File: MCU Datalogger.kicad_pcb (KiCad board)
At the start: 2 copper layers, 61 x 40.6 mm, 29 parts, among them J1 Conn_01x04_Pin, J2 Conn_01x04_Pin, J3 Conn_01x09_Pin, J4 Conn_02x03_Odd_Even, U1 24LC1025, U2 24LC1025, U3 DS1337S_, U4 ATMEGA328P-AU, Y1 16MHz, Y2 32.768 KHz

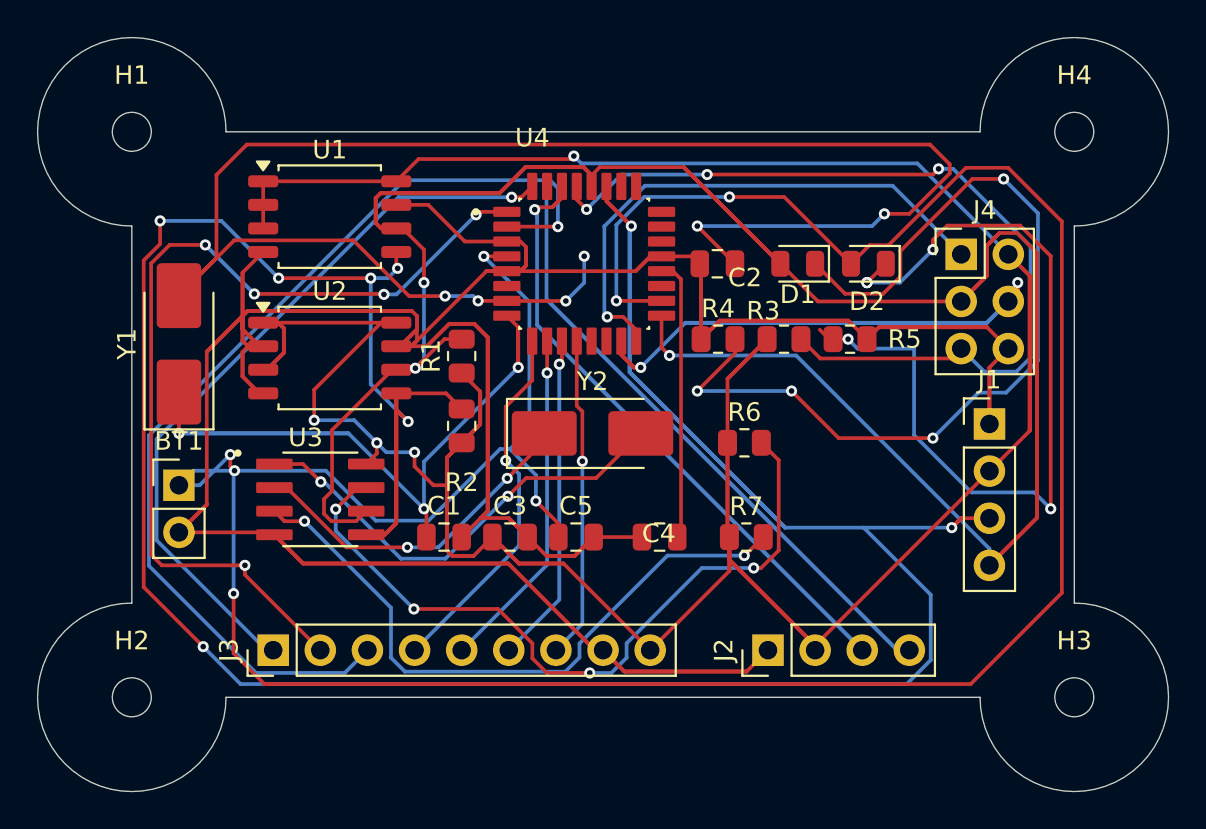
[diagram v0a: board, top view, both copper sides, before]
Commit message: Final 2-layered PCB with Logo
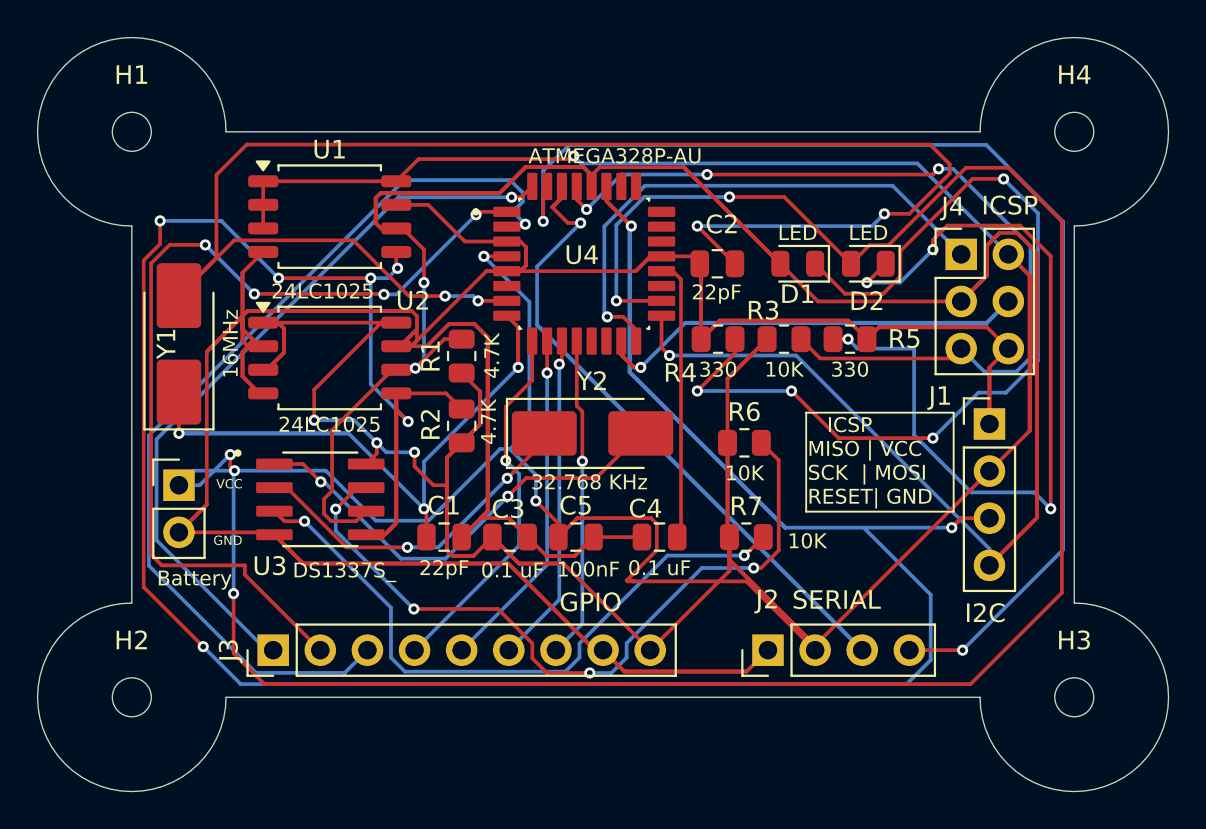
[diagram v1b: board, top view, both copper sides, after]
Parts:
- added REF**: KiCad-Logo2_12mm_SilkScreen, Symbol:KiCad-Logo2_12mm_SilkScreen, B.Cu at (109.5, 74.3)
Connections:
- BT1 pad 1: Net-(BT1-+) -> /VCC
- C5 pad 1: Net-(BT1-+) -> /VCC
- D2 pad 2: Net-(BT1-+) -> /VCC
- U4 pad 18: Net-(BT1-+) -> /VCC
- U4 pad 4: Net-(BT1-+) -> /VCC
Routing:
- net /VCC: track 201.0 -> 380.0 mm, vias 4 -> 11
- net Net-(BT1-+): track 157.5 -> 0.00 mm, vias 7 -> 0
- net Net-(U4-PB6): track 92.4 -> 86.4 mm, vias 6 -> 4
- net /TX: track 61.4 -> 65.2 mm, vias 0 -> 2
- net /D4: track 54.4 -> 50.9 mm
- net /RX: track 60.1 -> 61.2 mm
- net /MOSI: track 44.3 -> 43.3 mm, vias 2 -> 1
- net Net-(D2-K): track 46.4 -> 45.7 mm, vias 5 -> 4
- net /D3: vias 5 -> 4
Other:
- board text added: "* 2Mbit EEPROM * RTC * I2C,SPI, GPIOs"
- board text added: "Data Logger with the ATMega328P"
- board text added: "GND"
- board text added: "GPIO"
- board text added: "I2C"
- board text added: "ICSP"
- board text added: "ICSP MISO | VCC SCK | MOSI RESET| GND"
- board text added: "SERIAL"
- board text added: "VCC"

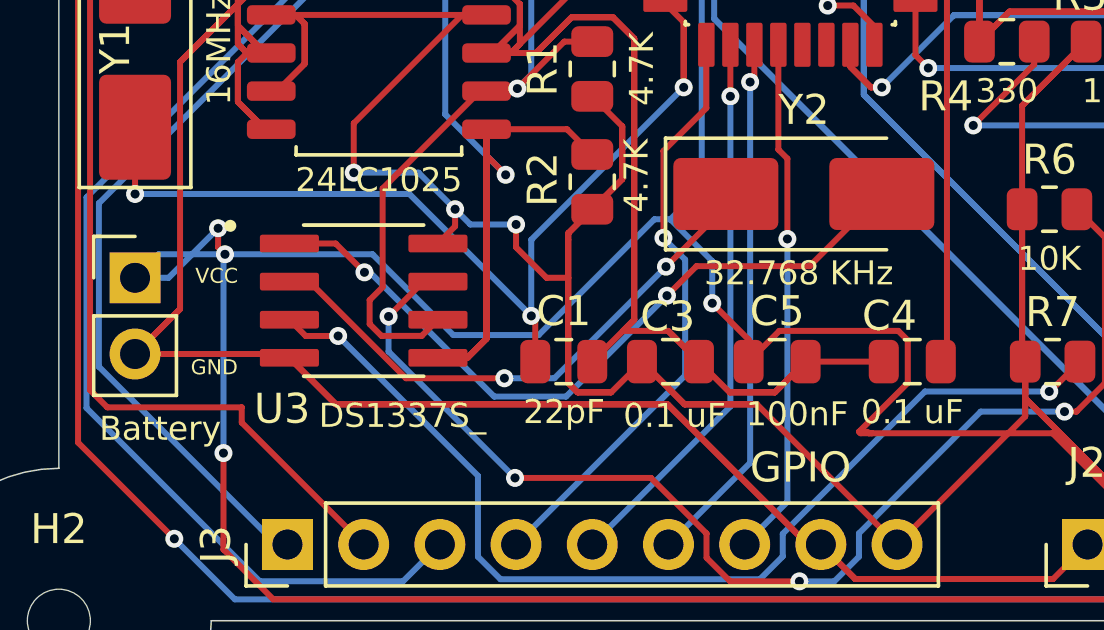
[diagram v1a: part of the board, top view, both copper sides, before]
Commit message: Completed 2-Layered PCB with Logo and 3D-shapes
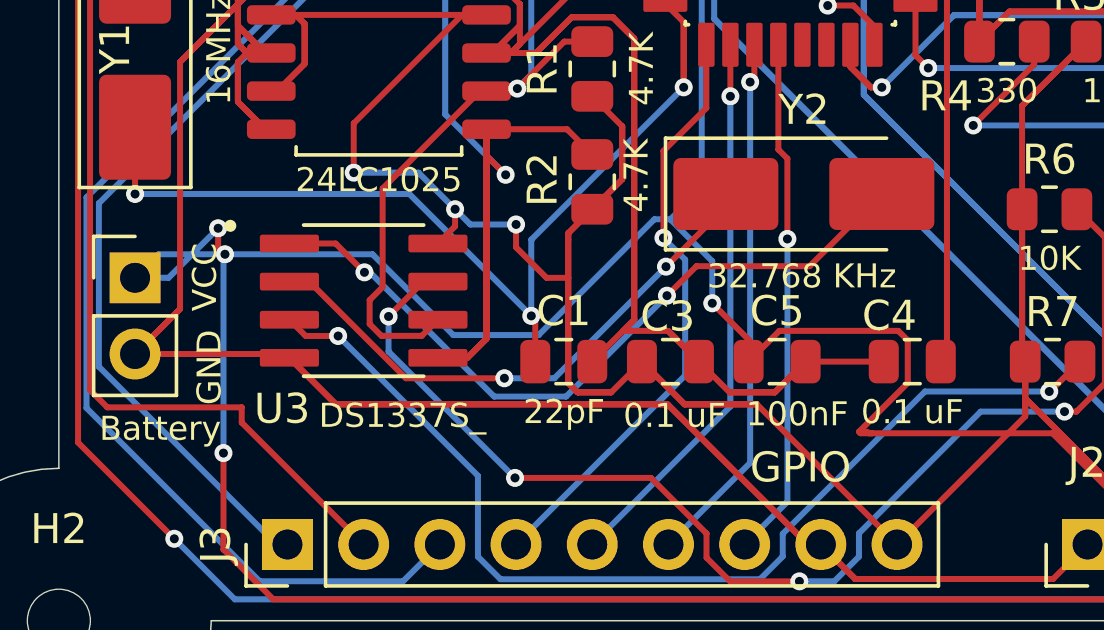
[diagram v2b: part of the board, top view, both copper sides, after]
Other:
- board text added: "By Josh"
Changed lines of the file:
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@@
 		)
 		(property "Value" "32.768 KHz"
-			(at -0.1686 2.6416 0)
+			(at -0.067 2.7432 0)
 			(layer "F.SilkS")
 			(effects
@@
 		)
 		(embedded_fonts no)
+		(model "${KICAD10_3DMODEL_DIR}/Package_SO.3dshapes/SOIC-8_3.9x4.9mm_P1.27mm.step"
+			(offset
+				(xyz 0 0 0)
+			)
+			(scale
+				(xyz 1 1 1)
+			)
+			(rotate
+				(xyz 0 0 0)
+			)
+		)
 	)
 	(footprint "Resistor_SMD:R_0805_2012Metric"
@@
 		)
 		(embedded_fonts no)
+		(model "${KICAD10_3DMODEL_DIR}/Package_QFP.3dshapes/TQFP-32_7x7mm_P0.8mm.step"
+			(offset
+				(xyz 0 0 0)
+			)
+			(scale
+				(xyz 1 1 1)
+			)
+			(rotate
+				(xyz 0 0 0)
+			)
+		)
 	)
 	(footprint "MountingHole:MountingHole_2.1mm"
@@
 		(layer "Edge.Cuts")
 	)
-	(gr_text "GND"
-		(at 85.6742 78.2066 0)
+	(gr_text "   ICSP\nMISO | VCC\nSCK  | MOSI\nRESET| GND"
+		(at 117.7036 76.0222 0)
 		(layer "F.SilkS")
 		(effects
 			(font
-				(size 0.5 0.5)
-				(thickness 0.01)
+				(size 0.8 0.8)
+				(thickness 0.1)
 			)
 			(justify left bottom)
 		)
 	)
-	(gr_text "VCC\n"
-		(at 85.8266 75.1586 0)
+	(gr_text "VCC"
+		(at 86.614 76.0476 90)
 		(layer "F.SilkS")
 		(effects
 			(font
-				(size 0.5 0.5)
-				(thickness 0.01)
+				(size 0.8 0.8)
+				(thickness 0.1)
 			)
 			(justify left bottom)
 		)
 	)
-	(gr_text "   ICSP\nMISO | VCC\nSCK  | MOSI\nRESET| GND"
-		(at 117.7036 76.0222 0)
+	(gr_text "GND"
+		(at 86.7664 79.1718 90)
 		(layer "F.SilkS")
 		(effects
@@
 	)
 	(gr_text "* 2Mbit EEPROM\n* RTC\n* I2C,SPI, GPIOs"
-		(at 124.1298 65.405 0)
+		(at 123.952 64.7446 0)
 		(layer "B.SilkS")
 		(effects
 			(font
-				(size 1.5 1.5)
+				(size 1.3 1.3)
 				(thickness 0.3)
 				(bold yes)
@@
 		)
 	)
+	(gr_text "By Josh"
+		(at 92.6338 81.7118 0)
+		(layer "B.SilkS")
+		(effects
+			(font
+				(size 1.5 1.5)
+				(thickness 0.3)
+				(bold yes)
+			)
+			(justify left bottom mirror)
+		)
+	)

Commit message: Modified Schematics
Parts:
- moved REF** 13.1 mm to (104.1, 62.4)
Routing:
- net /VCC: track 380.0 -> 226.0 mm, vias 11 -> 10
- net /SDA: track 185.1 -> 96.9 mm, vias 8 -> 10
- net GND: track 257.1 -> 173.8 mm, vias 0 -> 25
- net /SCK: track 157.5 -> 101.4 mm, vias 3 -> 11
- net Net-(D1-K): track 49.5 -> 6.41 mm, vias 4 -> 0
- net Net-(D2-K): track 45.7 -> 6.80 mm, vias 4 -> 2
- net Net-(U4-PB6): track 86.4 -> 48.2 mm, vias 4 -> 2
- net /TX: track 65.2 -> 38.7 mm, vias 2 -> 0
- net /RX: track 61.2 -> 36.2 mm, vias 1 -> 0
- net /D4: track 50.9 -> 28.1 mm, vias 1 -> 0
- net /D3: track 49.8 -> 28.9 mm, vias 4 -> 0
- net Net-(U3-X1): track 24.7 -> 44.0 mm, vias 2 -> 0
- net Net-(U3-X2): track 18.7 -> 36.9 mm, vias 2 -> 0
- net /MOSI: track 43.3 -> 26.3 mm, vias 1 -> 2
- net Net-(U4-PB7): track 43.0 -> 56.3 mm, vias 3 -> 4
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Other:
- copper layers 2 -> 4

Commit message: Fixed net bugs in 4 Layer PCB
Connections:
- J1 pad 4: /SCK -> /SCL
- R1 pad 2: /SCK -> /SCL
- U1 pad 6: /SCK -> /SCL
- U2 pad 6: /SCK -> /SCL
- U3 pad 6: /SCK -> /SCL
- U4 pad 28: /SCK -> /SCL
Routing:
- net /SCL: track 0.00 -> 81.6 mm, vias 0 -> 9
- net /SCK: track 101.4 -> 21.1 mm, vias 11 -> 4

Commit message: Added a custom made logo
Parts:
- added G***: LOGO, Custom made footprint:Custom made Footprint, B.Cu at (103.1, 82.5)
- moved REF** 1.71 mm to (105.7, 61.8)
